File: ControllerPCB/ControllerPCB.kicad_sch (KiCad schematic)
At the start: 110 parts, among them J1 Conn_02x40_Row_Letter_First, SW1 SW_SPDT, U1 LT1763CS8-1.8-PBF, U2 STM32F439ZITx, Y2 WE-XTAL_CFPX-218

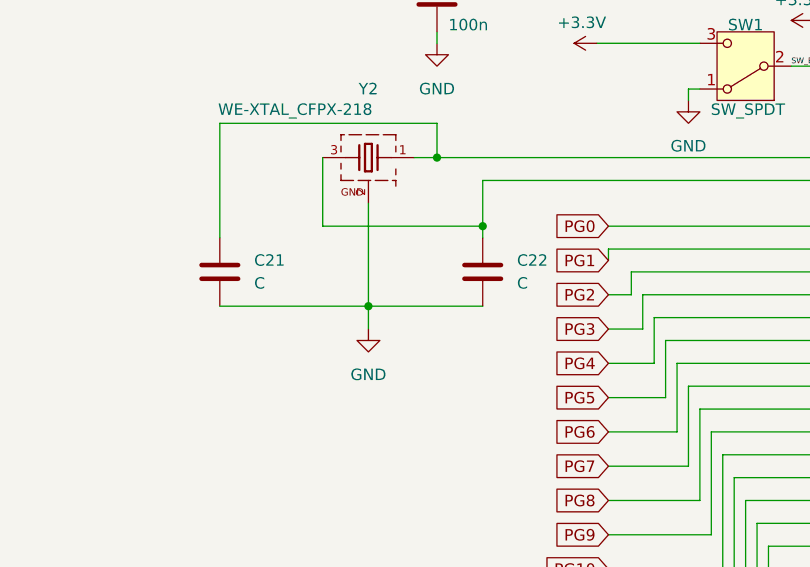
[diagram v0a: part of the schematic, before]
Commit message: Added footprints to the resistors and capacitors and values of Crystall Oscillator capacitors.
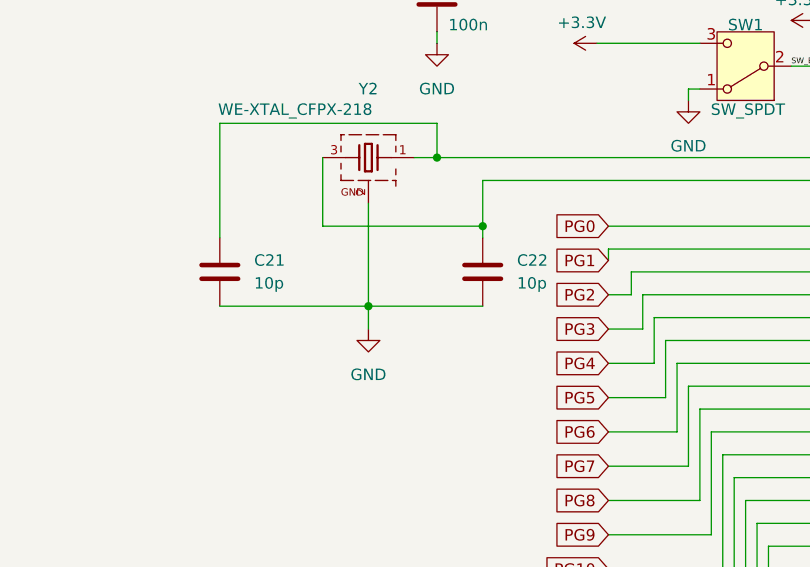
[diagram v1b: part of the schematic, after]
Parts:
- C21, C22: value C -> 10p; footprint (none) -> Capacitor_SMD:C_01005_0402Metric
- R17, R27, R28, R29, R30, R31, R32, R33, R34, R35, R36, R37, R38, R39, R40, R41, R42, R43, R44, R45, R46, R47, R48, R49, R50, R51, R52, R53, R54, R55, R56, R57, R58, R59, R60, R61, R62, R63, R64, R65, R66, R67, R68, R69, R70, R71, R72, R73, R74, R75, R76, R77, R78, R79, R80, R81: footprint (none) -> Resistor_SMD:R_1206_3216Metric
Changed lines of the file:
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@@
 			)
 		)
-		(property "Footprint" ""
+		(property "Footprint" "Resistor_SMD:R_1206_3216Metric"
 			(at 421.64 135.128 90)
 			(effects
@@
 			)
 		)
-		(property "Footprint" ""
+		(property "Footprint" "Resistor_SMD:R_1206_3216Metric"
 			(at 332.74 273.558 90)
 			(effects
@@
 			)
 		)
-		(property "Footprint" ""
+		(property "Footprint" "Resistor_SMD:R_1206_3216Metric"
 			(at 434.34 235.458 90)
 			(effects
@@
 			)
 		)
-		(property "Footprint" ""
+		(property "Footprint" "Resistor_SMD:R_1206_3216Metric"
 			(at 434.34 183.388 90)
 			(effects
@@
 			)
 		)
-		(property "Footprint" ""
+		(property "Footprint" "Resistor_SMD:R_1206_3216Metric"
 			(at 334.01 230.378 90)
 			(effects
@@
 			)
 		)
-		(property "Footprint" ""
+		(property "Footprint" "Resistor_SMD:R_1206_3216Metric"
 			(at 339.09 237.998 90)
 			(effects
@@
 			)
 		)
-		(property "Footprint" ""
+		(property "Footprint" "Resistor_SMD:R_1206_3216Metric"
 			(at 415.29 116.078 90)
 			(effects
@@
 			)
 		)
-		(property "Footprint" ""
+		(property "Footprint" "Resistor_SMD:R_1206_3216Metric"
 			(at 344.17 240.538 90)
 			(effects
@@
 			)
 		)
-		(property "Footprint" ""
+		(property "Footprint" "Resistor_SMD:R_1206_3216Metric"
 			(at 354.33 245.618 90)
 			(effects
@@
 			)
 		)
-		(property "Footprint" ""
+		(property "Footprint" "Resistor_SMD:R_1206_3216Metric"
 			(at 339.09 227.838 90)
 			(effects
@@
 			)
 		)
-		(property "Footprint" ""
+		(property "Footprint" "Resistor_SMD:R_1206_3216Metric"
 			(at 407.67 225.298 90)
 			(effects
@@
 			)
 		)
-		(property "Footprint" ""
+		(property "Footprint" "Resistor_SMD:R_1206_3216Metric"
 			(at 426.72 131.318 90)
 			(effects
@@
 			)
 		)
-		(property "Footprint" ""
+		(property "Footprint" "Resistor_SMD:R_1206_3216Metric"
 			(at 444.5 198.628 90)
 			(effects
@@
 			)
 		)
-		(property "Footprint" ""
+		(property "Footprint" "Resistor_SMD:R_1206_3216Metric"
 			(at 429.26 227.838 90)
 			(effects
@@
 			)
 		)
-		(property "Footprint" ""
+		(property "Footprint" "Resistor_SMD:R_1206_3216Metric"
 			(at 345.44 268.478 90)
 			(effects
@@
 			)
 		)
-		(property "Footprint" ""
+		(property "Footprint" "Resistor_SMD:R_1206_3216Metric"
 			(at 356.87 225.298 90)
 			(effects
@@
 			)
 		)
-		(property "Footprint" ""
+		(property "Footprint" "Resistor_SMD:R_1206_3216Metric"
 			(at 419.608 148.59 90)
 			(effects
@@
 			)
 		)
-		(property "Footprint" ""
+		(property "Footprint" "Resistor_SMD:R_1206_3216Metric"
 			(at 374.65 255.778 90)
 			(effects
@@
 			)
 		)
-		(property "Footprint" ""
+		(property "Footprint" "Resistor_SMD:R_1206_3216Metric"
 			(at 359.41 248.158 90)
 			(effects
@@
 			)
 		)
-		(property "Footprint" ""
+		(property "Footprint" "Resistor_SMD:R_1206_3216Metric"
 			(at 364.49 250.698 90)
 			(effects
@@
 			)
 		)
-		(property "Footprint" ""
+		(property "Footprint" "Resistor_SMD:R_1206_3216Metric"
 			(at 349.25 243.078 90)
 			(effects
@@
 			)
 		)
-		(property "Footprint" ""
+		(property "Footprint" "Resistor_SMD:R_1206_3216Metric"
 			(at 358.14 263.398 90)
 			(effects
@@
 			)
 		)
-		(property "Footprint" ""
+		(property "Footprint" "Resistor_SMD:R_1206_3216Metric"
 			(at 415.29 127.508 90)
 			(effects
@@
 			)
 		)
-		(property "Footprint" ""
+		(property "Footprint" "Resistor_SMD:R_1206_3216Metric"
 			(at 424.688 168.91 90)
 			(effects
@@
 			)
 		)
-		(property "Footprint" ""
+		(property "Footprint" "Resistor_SMD:R_1206_3216Metric"
 			(at 421.64 230.378 90)
 			(effects
@@
 			)
 		)
-		(property "Footprint" ""
+		(property "Footprint" "Resistor_SMD:R_1206_3216Metric"
 			(at 426.72 156.718 90)
 			(effects
@@
 			)
 		)
-		(property "Footprint" ""
+		(property "Footprint" "Resistor_SMD:R_1206_3216Metric"
 			(at 350.52 227.838 90)
 			(effects
@@
 			)
 		)
-		(property "Footprint" ""
+		(property "Footprint" "Resistor_SMD:R_1206_3216Metric"
 			(at 327.66 276.098 90)
 			(effects
@@
 			)
 		)
-		(property "Footprint" ""
+		(property "Footprint" "Resistor_SMD:R_1206_3216Metric"
 			(at 421.64 123.698 90)
 			(effects
@@
 			)
 		)
-		(property "Footprint" ""
+		(property "Footprint" "Resistor_SMD:R_1206_3216Metric"
 			(at 417.83 220.218 90)
 			(effects
@@
 			)
 		)
-		(property "Footprint" ""
+		(property "Footprint" "Resistor_SMD:R_1206_3216Metric"
 			(at 427.99 150.368 90)
 			(effects
@@
 			)
 		)
-		(property "Footprint" ""
+		(property "Footprint" "Resistor_SMD:R_1206_3216Metric"
 			(at 426.72 142.748 90)
 			(effects
@@
 			)
 		)
-		(property "Footprint" ""
+		(property "Footprint" "Resistor_SMD:R_1206_3216Metric"
 			(at 436.118 204.47 90)
 			(effects
@@
 			)
 		)
-		(property "Footprint" ""
+		(property "Footprint" "Resistor_SMD:R_1206_3216Metric"
 			(at 412.75 222.758 90)
 			(effects
@@
 			)
 		)
-		(property "Footprint" ""
+		(property "Footprint" "Resistor_SMD:R_1206_3216Metric"
 			(at 425.45 108.458 90)
 			(effects
@@
 			)
 		)
-		(property "Footprint" ""
+		(property "Footprint" "Resistor_SMD:R_1206_3216Metric"
 			(at 417.068 140.97 90)
 			(effects
@@
 			)
 		)
-		(property "Footprint" ""
+		(property "Footprint" "Resistor_SMD:R_1206_3216Metric"
 			(at 351.79 265.938 90)
 			(effects
@@
 			)
 		)
-		(property "Footprint" ""
+		(property "Footprint" "Resistor_SMD:R_1206_3216Metric"
 			(at 379.73 258.318 90)
 			(effects
@@
 			)
 		)
-		(property "Footprint" ""
+		(property "Footprint" "Resistor_SMD:R_1206_3216Metric"
 			(at 364.49 260.858 90)
 			(effects
@@
 			)
 		)
-		(property "Footprint" ""
+		(property "Footprint" "Resistor_SMD:R_1206_3216Metric"
 			(at 378.46 220.218 90)
 			(effects
@@
 			)
 		)
-		(property "Footprint" ""
+		(property "Footprint" "Resistor_SMD:R_1206_3216Metric"
 			(at 353.06 189.738 90)
 			(effects
@@
 			)
 		)
-		(property "Footprint" ""
+		(property "Footprint" "Resistor_SMD:R_1206_3216Metric"
 			(at 423.418 161.29 90)
 			(effects
@@
 			)
 		)
-		(property "Value" "C"
+		(property "Value" "10p"
 			(at 209.55 138.4299 0)
 			(effects
@@
 			)
 		)
-		(property "Footprint" ""
+		(property "Footprint" "Capacitor_SMD:C_01005_0402Metric"
 			(at 206.7052 140.97 0)
 			(effects
@@
 			)
 		)
-		(property "Footprint" ""
+		(property "Footprint" "Resistor_SMD:R_1206_3216Metric"
 			(at 426.72 119.888 90)
 			(effects
@@
 			)
 		)
-		(property "Footprint" ""
+		(property "Footprint" "Resistor_SMD:R_1206_3216Metric"
 			(at 444.5 175.768 90)
 			(effects
@@
 			)
 		)
-		(property "Footprint" ""
+		(property "Footprint" "Resistor_SMD:R_1206_3216Metric"
 			(at 422.91 217.678 90)
 			(effects
@@
 			)
 		)
-		(property "Footprint" ""
+		(property "Footprint" "Resistor_SMD:R_1206_3216Metric"
 			(at 444.5 187.198 90)
 			(effects
@@
 			)
 		)
-		(property "Footprint" ""
+		(property "Footprint" "Resistor_SMD:R_1206_3216Metric"
 			(at 363.22 222.758 90)
 			(effects
@@
 			)
 		)
-		(property "Footprint" ""
+		(property "Footprint" "Resistor_SMD:R_1206_3216Metric"
 			(at 339.09 271.018 90)
 			(effects
@@
 			)
 		)
-		(property "Footprint" ""
+		(property "Footprint" "Resistor_SMD:R_1206_3216Metric"
 			(at 420.37 112.268 90)
 			(effects
@@
 			)
 		)
-		(property "Footprint" ""
+		(property "Footprint" "Resistor_SMD:R_1206_3216Metric"
 			(at 439.42 191.008 90)
 			(effects
@@
 			)
 		)
-		(property "Footprint" ""
+		(property "Footprint" "Resistor_SMD:R_1206_3216Metric"
 			(at 415.29 232.918 90)
 			(effects
@@
 			)
 		)
-		(property "Footprint" ""
+		(property "Footprint" "Resistor_SMD:R_1206_3216Metric"
 			(at 327.66 232.918 90)
 			(effects
@@
 			)
 		)
-		(property "Footprint" ""
+		(property "Footprint" "Resistor_SMD:R_1206_3216Metric"
 			(at 425.958 176.53 90)
 			(effects
@@
 			)
 		)
-		(property "Footprint" ""
+		(property "Footprint" "Resistor_SMD:R_1206_3216Metric"
 			(at 439.42 179.578 90)
 			(effects
@@
 			)
 		)
-		(property "Footprint" ""
+		(property "Footprint" "Resistor_SMD:R_1206_3216Metric"
 			(at 433.578 196.85 90)
 			(effects
@@
 			)
 		)
-		(property "Value" "C"
+		(property "Value" "10p"
 			(at 180.34 138.4299 0)
 			(effects
@@
 			)
 		)
-		(property "Footprint" ""
+		(property "Footprint" "Capacitor_SMD:C_01005_0402Metric"
 			(at 177.4952 140.97 0)
 			(effects
@@
 			)
 		)
-		(property "Footprint" ""
+		(property "Footprint" "Resistor_SMD:R_1206_3216Metric"
 			(at 369.57 253.238 90)
 			(effects

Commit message: grant test commit
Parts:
- added C23: C, symbol Device:C
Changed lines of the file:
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@@
+	)
+	(symbol
+		(lib_id "Device:C")
+		(at 162.56 40.64 0)
+		(unit 1)
+		(exclude_from_sim no)
+		(in_bom yes)
+		(on_board yes)
+		(dnp no)
+		(fields_autoplaced yes)
+		(property "Reference" "C23"
+			(at 166.37 39.3699 0)
+			(effects
+				(font
+					(size 1.27 1.27)
+				)
+				(justify left)
+			)
+		)
+		(property "Value" "C"
+			(at 166.37 41.9099 0)
+			(effects
+				(font
+					(size 1.27 1.27)
+				)
+				(justify left)
+			)
+		)
+		(property "Footprint" ""
+			(at 163.5252 44.45 0)
+			(effects
+				(font
+					(size 1.27 1.27)
+				)
+				(hide yes)
+			)
+		)
+		(property "Datasheet" "~"
+			(at 162.56 40.64 0)
+			(effects
+				(font
+					(size 1.27 1.27)
+				)
+				(hide yes)
+			)
+		)
+		(property "Description" "Unpolarized capacitor"
+			(at 162.56 40.64 0)
+			(effects
+				(font
+					(size 1.27 1.27)
+				)
+				(hide yes)
+			)
+		)
+		(pin "1"
+		)
+		(pin "2"
+		)
+		(instances
+			(project ""
+				(path "/b6b9154e-ee88-44ea-8b68-6c4328b55066"
+					(reference "C23")
+					(unit 1)
+				)
+			)
+		)
 	)
 	(symbol

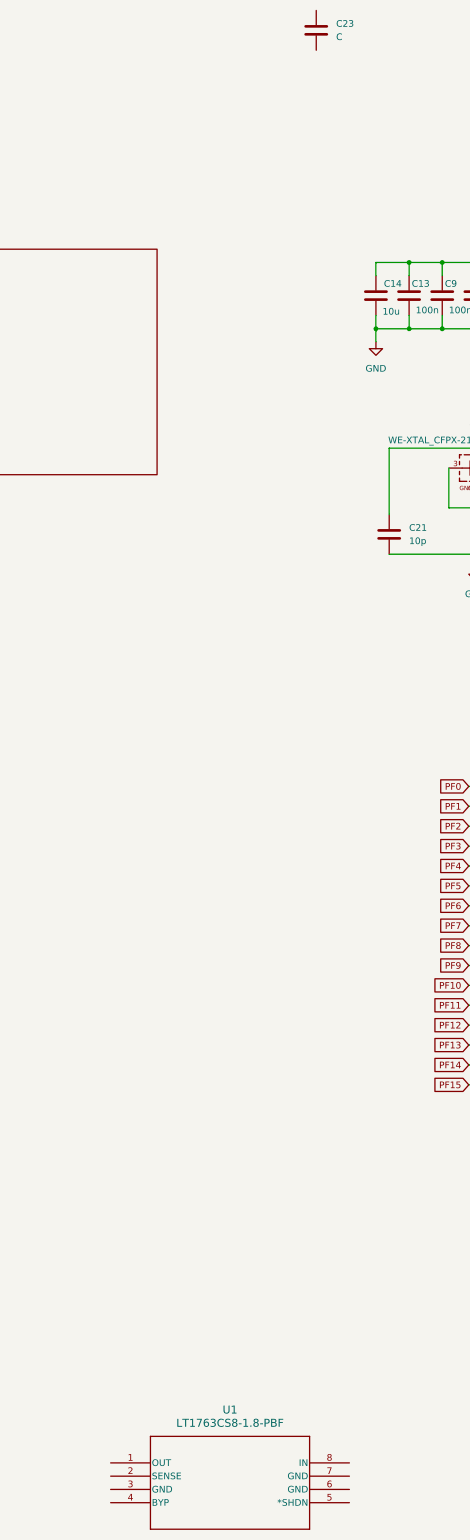
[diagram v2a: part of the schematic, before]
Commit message: Power_Connector
Power portion added
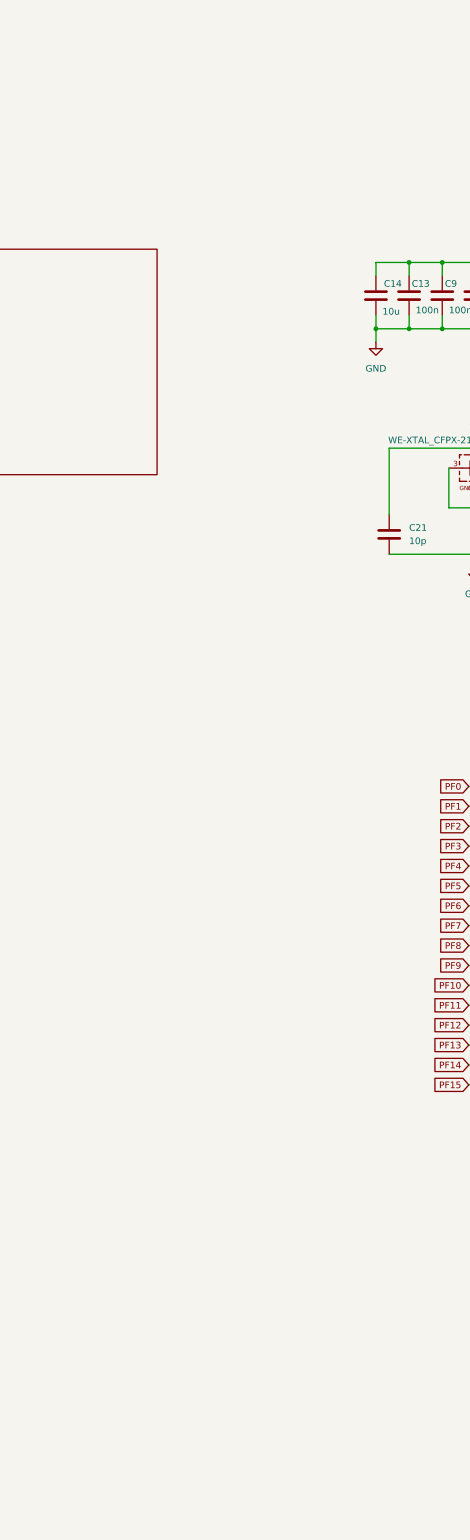
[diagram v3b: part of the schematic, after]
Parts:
- removed C23: C, symbol Device:C
- removed U1: LT1763CS8-1.8-PBF, SO-8_S_LIT, symbol LDO1763:LT1763CS8-1.8-PBF
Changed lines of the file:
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@@
-	)
-	(symbol
-		(lib_id "LDO1763:LT1763CS8-1.8-PBF")
-		(at 123.19 314.96 0)
-		(unit 1)
-		(exclude_from_sim no)
-		(in_bom yes)
-		(on_board yes)
-		(dnp no)
-		(fields_autoplaced yes)
-		(property "Reference" "U1"
-			(at 146.05 304.8 0)
-			(effects
-				(font
-					(size 1.524 1.524)
-				)
-			)
-		)
-		(property "Value" "LT1763CS8-1.8-PBF"
-			(at 146.05 307.34 0)
-			(effects
-				(font
-					(size 1.524 1.524)
-				)
-			)
-		)
-		(property "Footprint" "SO-8_S_LIT"
-			(at 123.19 314.96 0)
-			(effects
-				(font
-					(size 1.27 1.27)
-					(italic yes)
-				)
-				(hide yes)
-			)
-		)
-		(property "Datasheet" "LT1763CS8-1.8-PBF"
-			(at 123.19 314.96 0)
-			(effects
-				(font
-					(size 1.27 1.27)
-					(italic yes)
-				)
-				(hide yes)
-			)
-		)
-		(property "Description" ""
-			(at 123.19 314.96 0)
-			(effects
-				(font
-					(size 1.27 1.27)
-				)
-				(hide yes)
-			)
-		)
-		(pin "4"
-		)
-		(pin "8"
-		)
-		(pin "2"
-		)
-		(pin "1"
-		)
-		(pin "6"
-		)
-		(pin "7"
-		)
-		(pin "5"
-		)
-		(pin "3"
-		)
-		(instances
-			(project "ControllerPCB"
-				(path "/b6b9154e-ee88-44ea-8b68-6c4328b55066"
-					(reference "U1")
-					(unit 1)
-				)
-			)
-		)
 	)
 	(symbol
@@
 					(unit 1)
 				)
-			)
-		)
-	)
-	(symbol
-		(lib_id "Device:C")
-		(at 162.56 40.64 0)
-		(unit 1)
-		(exclude_from_sim no)
-		(in_bom yes)
-		(on_board yes)
-		(dnp no)
-		(fields_autoplaced yes)
-		(property "Reference" "C23"
-			(at 166.37 39.3699 0)
-			(effects
-				(font
-					(size 1.27 1.27)
-				)
-				(justify left)
-			)
-		)
-		(property "Value" "C"
-			(at 166.37 41.9099 0)
-			(effects
-				(font
-					(size 1.27 1.27)
-				)
-				(justify left)
-			)
-		)
-		(property "Footprint" ""
-			(at 163.5252 44.45 0)
-			(effects
-				(font
-					(size 1.27 1.27)
-				)
-				(hide yes)
-			)
-		)
-		(property "Datasheet" "~"
-			(at 162.56 40.64 0)
-			(effects
-				(font
-					(size 1.27 1.27)
-				)
-				(hide yes)
-			)
-		)
-		(property "Description" "Unpolarized capacitor"
-			(at 162.56 40.64 0)
-			(effects
-				(font
-					(size 1.27 1.27)
-				)
-				(hide yes)
-			)
-		)
-		(pin "1"
-		)
-		(pin "2"
-		)
-		(instances
-			(project ""
-				(path "/b6b9154e-ee88-44ea-8b68-6c4328b55066"
-					(reference "C23")
-					(unit 1)
-				)
